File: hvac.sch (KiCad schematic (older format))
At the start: 35 parts, among them CN1 1X4-3.5MM, IC1 ATMEGA328P-A, J1 PROGRAMMING HEADER, J2 SERIAL PORT, J3 POWER_INPUT, J4 1X2-3.5MM, SW1 SPST, SW2 SPST, SW3 SPST, U1 MIC5225

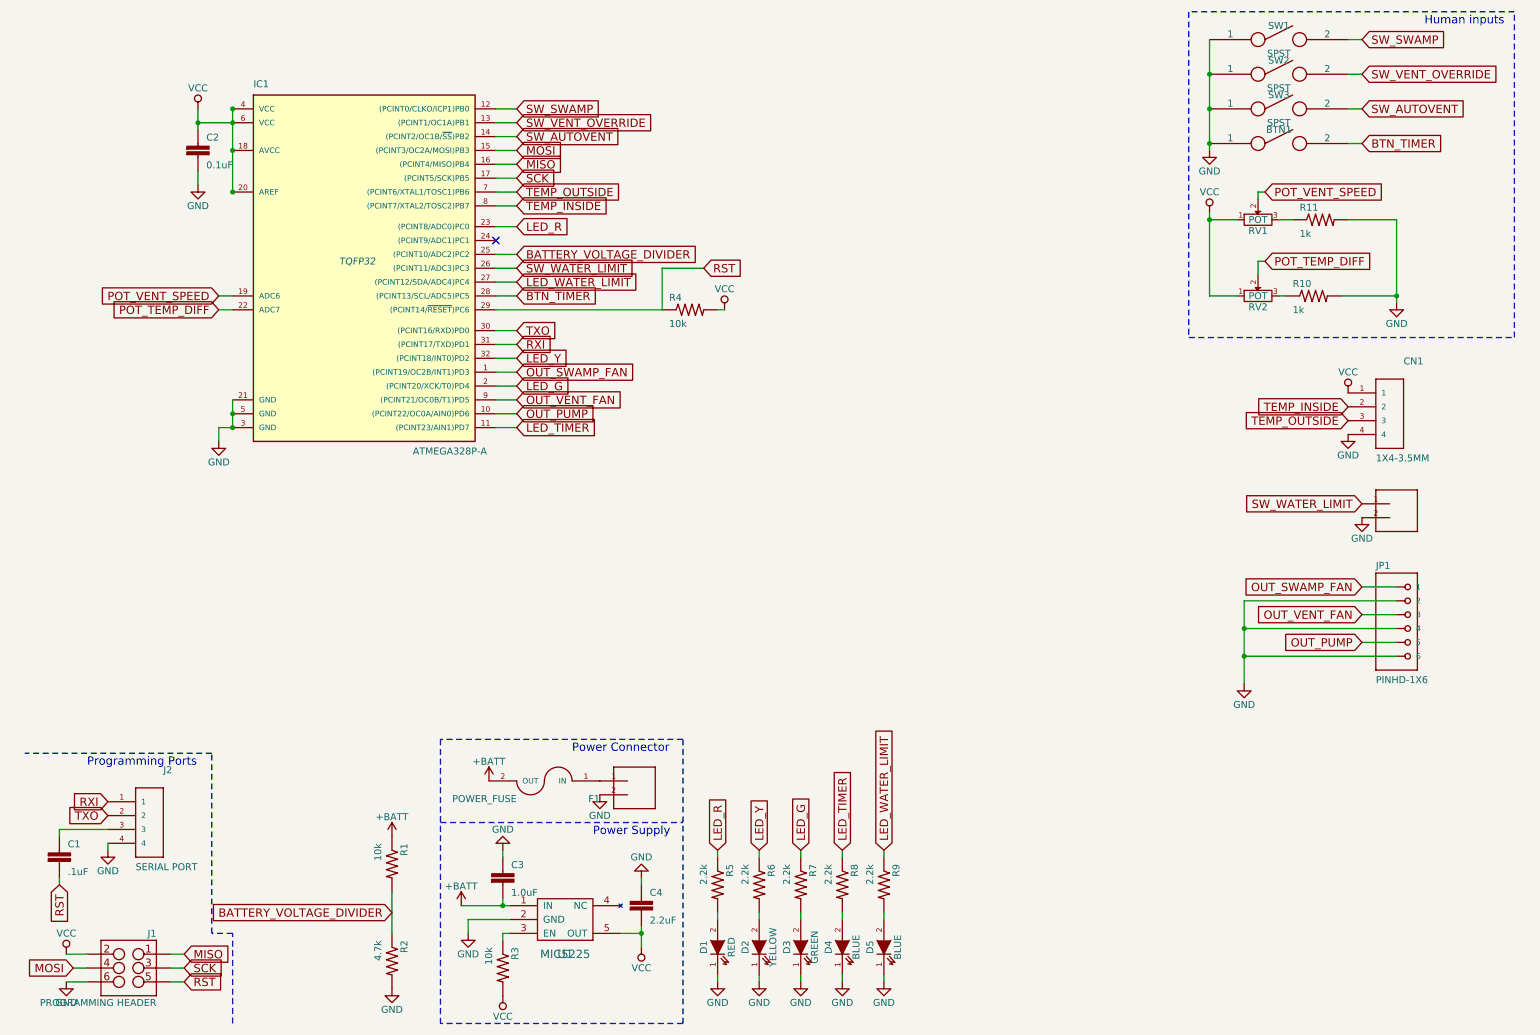
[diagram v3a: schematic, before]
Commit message: Add mosfets for driving fans and pump
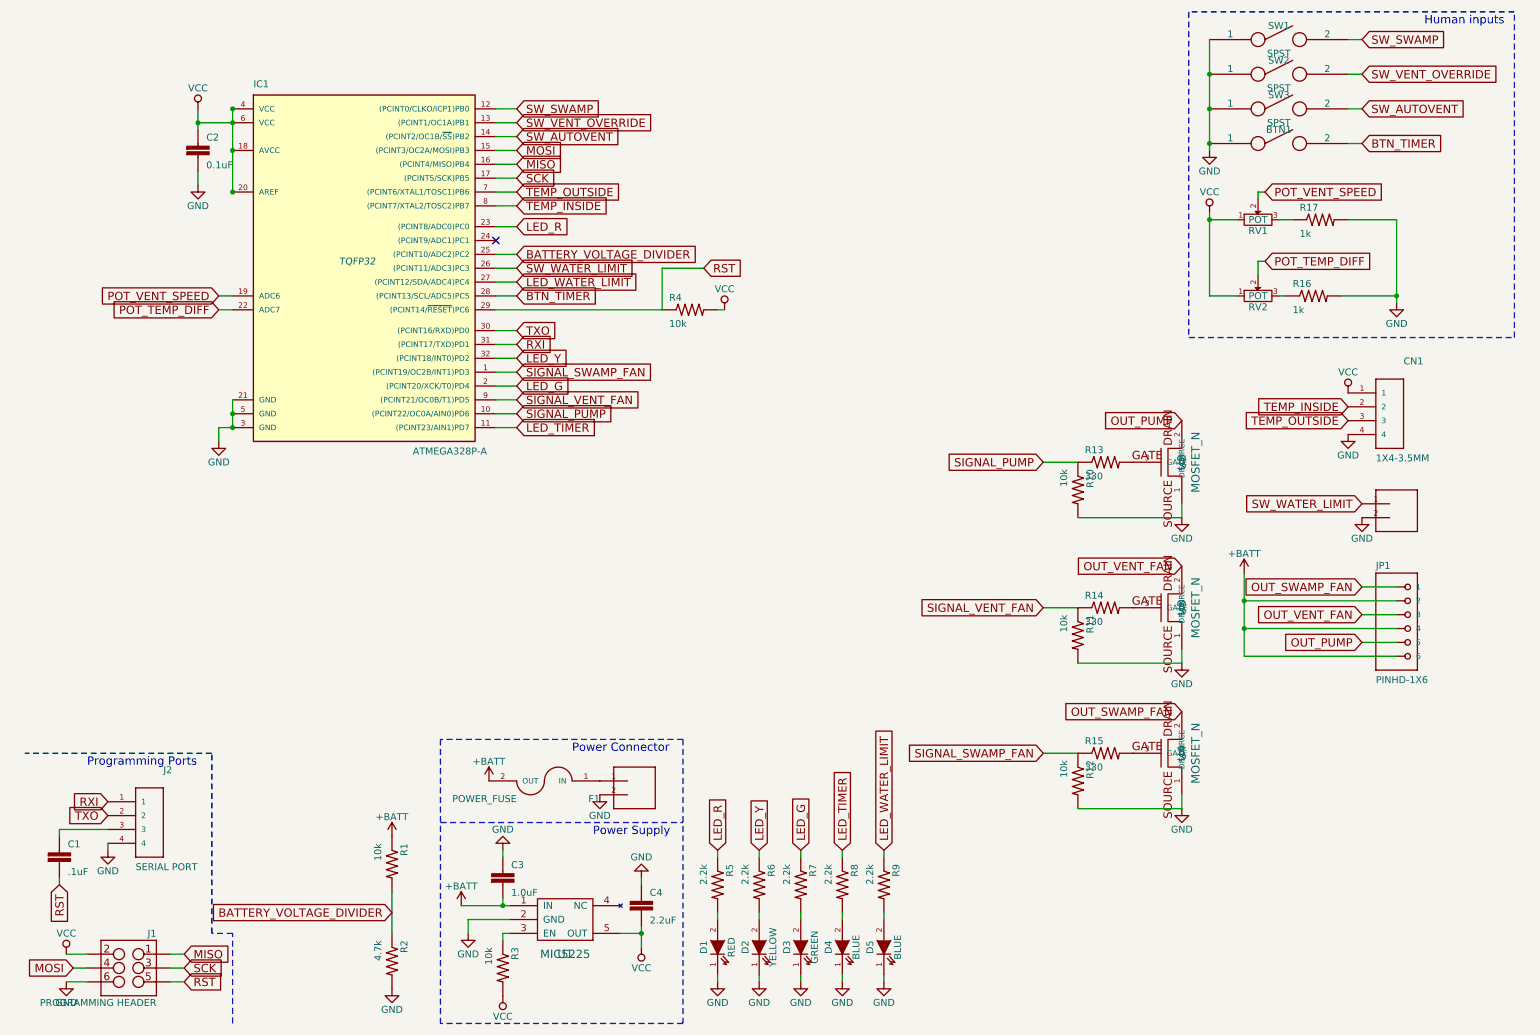
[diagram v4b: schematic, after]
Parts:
- added R10, R11, R12: 10k, 0402-RES, symbol RESISTOR0402
- added R13, R14, R15: 330, 0402-RES, symbol RESISTOR0402
- added U2, U3, U4: MOSFET_N, symbol MOSFET_N
- renumbered R10 to R16, R11 to R17
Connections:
- net +BATT: now also JP1.2, JP1.4, JP1.6
- net GND: now also R10.2, R11.2, R12.2, U2.1 (SOURCE), U3.1 (SOURCE), U4.1 (SOURCE); no longer JP1.2, JP1.4, JP1.6
- net OUT_PUMP: now also U2.2 (DRAIN); no longer IC1.10 ((PCINT22/OC0A/AIN0)PD6)
- net OUT_SWAMP_FAN: now also U4.2 (DRAIN); no longer IC1.1 ((PCINT19/OC2B/INT1)PD3)
- net OUT_VENT_FAN: now also U3.2 (DRAIN); no longer IC1.9 ((PCINT21/OC0B/T1)PD5)
- new net: R14.2, U3.3 (GATE)
- new net: R15.2, U4.3 (GATE)
- new net: R13.2, U2.3 (GATE)
- new net SIGNAL_PUMP: IC1.10 ((PCINT22/OC0A/AIN0)PD6), R10.1, R13.1
- new net SIGNAL_SWAMP_FAN: IC1.1 ((PCINT19/OC2B/INT1)PD3), R12.1, R15.1
- new net SIGNAL_VENT_FAN: IC1.9 ((PCINT21/OC0B/T1)PD5), R11.1, R14.1
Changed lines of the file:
@@
 	9350 1800 9400 1800
 $Comp
-L RESISTOR0402 R11
+L RESISTOR0402 R17
 U 1 1 590F04F0
 P 9800 2000
-F 0 "R11" H 9650 2059 50  0000 L BNN
+F 0 "R17" H 9650 2059 50  0000 L BNN
 F 1 "1k" H 9650 1870 50  0000 L BNN
 F 2 "0402-RES" H 9830 2150 20  0001 C CNN
@@
 	10350 2000 10000 2000
 $Comp
-L RESISTOR0402 R10
+L RESISTOR0402 R16
 U 1 1 590F06BC
 P 9750 2550
-F 0 "R10" H 9600 2609 50  0000 L BNN
+F 0 "R16" H 9600 2609 50  0000 L BNN
 F 1 "1k" H 9600 2420 50  0000 L BNN
 F 2 "0402-RES" H 9780 2700 20  0001 C CNN
@@
 	3850 3400 4000 3400
 Text GLabel 4000 3100 2    60   Input ~ 0
-OUT_SWAMP_FAN
+SIGNAL_SWAMP_FAN
 Text GLabel 4000 3300 2    60   Input ~ 0
-OUT_VENT_FAN
+SIGNAL_VENT_FAN
 Text GLabel 4000 3400 2    60   Input ~ 0
-OUT_PUMP
+SIGNAL_PUMP
 Text GLabel 4000 1200 2    60   Input ~ 0
 SW_SWAMP
@@
 Text GLabel 10100 4050 0    60   Input ~ 0
 SW_WATER_LIMIT
-Text GLabel 10100 4650 0    60   Input ~ 0
-OUT_SWAMP_FAN
+Text GLabel 7800 4800 0    60   Input ~ 0
+SIGNAL_VENT_FAN
 Text GLabel 10100 4850 0    60   Input ~ 0
 OUT_VENT_FAN
@@
 Wire Wire Line
 	10100 5050 10350 5050
-$Comp
-L GND #PWR029
-U 1 1 590FF3B2
-P 9250 5350
-F 0 "#PWR029" H 9250 5100 50  0001 C CNN
-F 1 "GND" H 9250 5200 50  0000 C CNN
-F 2 "" H 9250 5350 50  0000 C CNN
-F 3 "" H 9250 5350 50  0000 C CNN
-	1    9250 5350
-	1    0    0    -1
-$EndComp
-Wire Wire Line
-	9250 5350 9250 4750
-Wire Wire Line
-	9250 4750 10350 4750
-Wire Wire Line
-	10350 4950 9250 4950
-Connection ~ 9250 4950
-Wire Wire Line
-	10350 5150 9250 5150
-Connection ~ 9250 5150
 Connection ~ 9000 1450
 $Comp
@@
 	-1   0    0    1
 $EndComp
+$Comp
+L MOSFET_N U3
+U 1 1 59102281
+P 8900 4800
+F 0 "U3" H 8900 4900 60  0000 C CNN
+F 1 "MOSFET_N" H 8900 4800 60  0000 C CNN
+F 2 "" H 8900 4750 60  0000 C CNN
+F 3 "" H 8900 4750 60  0000 C CNN
+	1    8900 4800
+	0    -1   -1   0
+$EndComp
+$Comp
+L GND #PWR029
+U 1 1 59102A56
+P 8800 5200
+F 0 "#PWR029" H 8800 4950 50  0001 C CNN
+F 1 "GND" H 8800 5050 50  0000 C CNN
+F 2 "" H 8800 5200 50  0000 C CNN
+F 3 "" H 8800 5200 50  0000 C CNN
+	1    8800 5200
+	1    0    0    -1
+$EndComp
+$Comp
+L +BATT #PWR030
+U 1 1 59102C3A
+P 9250 4550
+F 0 "#PWR030" H 9250 4400 50  0001 C CNN
+F 1 "+BATT" H 9250 4690 50  0000 C CNN
+F 2 "" H 9250 4550 50  0000 C CNN
+F 3 "" H 9250 4550 50  0000 C CNN
+	1    9250 4550
+	1    0    0    -1
+$EndComp
+$Comp
+L RESISTOR0402 R14
+U 1 1 59102F73
+P 8250 4800
+F 0 "R14" H 8100 4859 50  0000 L BNN
+F 1 "330" H 8100 4670 50  0000 L BNN
+F 2 "0402-RES" H 8280 4950 20  0001 C CNN
+F 3 "" H 8250 4800 60  0000 C CNN
+	1    8250 4800
+	1    0    0    -1
+$EndComp
+$Comp
+L RESISTOR0402 R11
+U 1 1 591032B1
+P 8050 5000
+F 0 "R11" H 7900 5059 50  0000 L BNN
+F 1 "10k" H 7900 4870 50  0000 L BNN
+F 2 "0402-RES" H 8080 5150 20  0001 C CNN
+F 3 "" H 8050 5000 60  0000 C CNN
+	1    8050 5000
+	0    1    1    0
+$EndComp
+Wire Wire Line
+	7800 4800 8050 4800
+Text GLabel 8800 4500 0    60   Input ~ 0
+OUT_VENT_FAN
+Text GLabel 10100 4650 0    60   Input ~ 0
+OUT_SWAMP_FAN
+Wire Wire Line
+	9250 4550 9250 5150
+Wire Wire Line
+	9250 5150 10350 5150
+Wire Wire Line
+	10350 4950 9250 4950
+Connection ~ 9250 4950
+Wire Wire Line
+	9250 4750 10350 4750
+Connection ~ 9250 4750
+Wire Wire Line
+	8800 5100 8800 5200
+Text GLabel 7800 5850 0    60   Input ~ 0
+SIGNAL_SWAMP_FAN
+$Comp
+L MOSFET_N U4
+U 1 1 591065E0
+P 8900 5850
+F 0 "U4" H 8900 5950 60  0000 C CNN
+F 1 "MOSFET_N" H 8900 5850 60  0000 C CNN
+F 2 "" H 8900 5800 60  0000 C CNN
+F 3 "" H 8900 5800 60  0000 C CNN
+	1    8900 5850
+	0    -1   -1   0
+$EndComp
+$Comp
+L GND #PWR031
+U 1 1 591065E6
+P 8800 6250
+F 0 "#PWR031" H 8800 6000 50  0001 C CNN
+F 1 "GND" H 8800 6100 50  0000 C CNN
+F 2 "" H 8800 6250 50  0000 C CNN
+F 3 "" H 8800 6250 50  0000 C CNN
+	1    8800 6250
+	1    0    0    -1
+$EndComp
+$Comp
+L RESISTOR0402 R15
+U 1 1 591065EC
+P 8250 5850
+F 0 "R15" H 8100 5909 50  0000 L BNN
+F 1 "330" H 8100 5720 50  0000 L BNN
+F 2 "0402-RES" H 8280 6000 20  0001 C CNN
+F 3 "" H 8250 5850 60  0000 C CNN
+	1    8250 5850
+	1    0    0    -1
+$EndComp
+$Comp
+L RESISTOR0402 R12
+U 1 1 591065F2
+P 8050 6050
+F 0 "R12" H 7900 6109 50  0000 L BNN
+F 1 "10k" H 7900 5920 50  0000 L BNN
+F 2 "0402-RES" H 8080 6200 20  0001 C CNN
+F 3 "" H 8050 6050 60  0000 C CNN
+	1    8050 6050
+	0    1    1    0
+$EndComp
+Wire Wire Line
+	7800 5850 8050 5850
+Text GLabel 8800 5550 0    60   Input ~ 0
+OUT_SWAMP_FAN
+Wire Wire Line
+	8800 6250 8050 6250
+Wire Wire Line
+	8800 6150 8800 6250
+Text GLabel 7800 3750 0    60   Input ~ 0
+SIGNAL_PUMP
+$Comp
+L MOSFET_N U2
+U 1 1 591067AD
+P 8900 3750
+F 0 "U2" H 8900 3850 60  0000 C CNN
+F 1 "MOSFET_N" H 8900 3750 60  0000 C CNN
+F 2 "" H 8900 3700 60  0000 C CNN
+F 3 "" H 8900 3700 60  0000 C CNN
+	1    8900 3750
+	0    -1   -1   0
+$EndComp
+$Comp
+L GND #PWR032
+U 1 1 591067B3
+P 8800 4150
+F 0 "#PWR032" H 8800 3900 50  0001 C CNN
+F 1 "GND" H 8800 4000 50  0000 C CNN
+F 2 "" H 8800 4150 50  0000 C CNN
+F 3 "" H 8800 4150 50  0000 C CNN
+	1    8800 4150
+	1    0    0    -1
+$EndComp
+$Comp
+L RESISTOR0402 R13
+U 1 1 591067B9
+P 8250 3750
+F 0 "R13" H 8100 3809 50  0000 L BNN
+F 1 "330" H 8100 3620 50  0000 L BNN
+F 2 "0402-RES" H 8280 3900 20  0001 C CNN
+F 3 "" H 8250 3750 60  0000 C CNN
+	1    8250 3750
+	1    0    0    -1
+$EndComp
+$Comp
+L RESISTOR0402 R10
+U 1 1 591067BF
+P 8050 3950
+F 0 "R10" H 7900 4009 50  0000 L BNN
+F 1 "10k" H 7900 3820 50  0000 L BNN
+F 2 "0402-RES" H 8080 4100 20  0001 C CNN
+F 3 "" H 8050 3950 60  0000 C CNN
+	1    8050 3950
+	0    1    1    0
+$EndComp
+Wire Wire Line
+	7800 3750 8050 3750
+Text GLabel 8800 3450 0    60   Input ~ 0
+OUT_PUMP
+Wire Wire Line
+	8800 4150 8050 4150
+Wire Wire Line
+	8800 4050 8800 4150
+Wire Wire Line
+	8800 5200 8050 5200
 $EndSCHEMATC

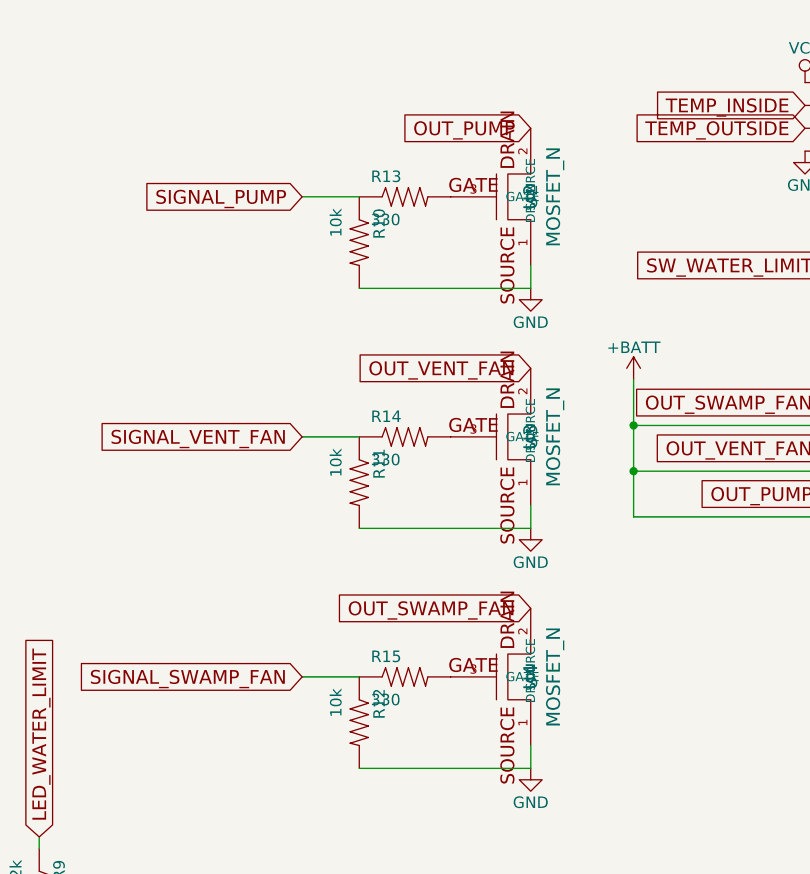
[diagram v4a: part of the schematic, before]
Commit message: Switch to 220ohm resistors
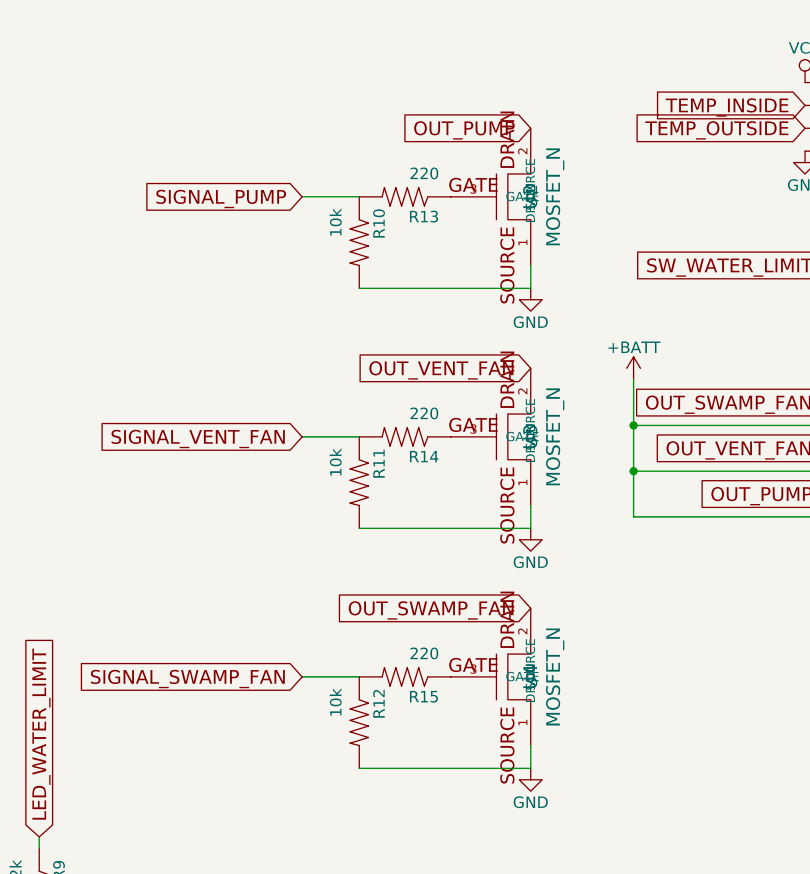
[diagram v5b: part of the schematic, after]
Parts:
- R13, R14, R15: value 330 -> 220
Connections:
- net SIGNAL_PUMP: now also R13.2; no longer R13.1
- net SIGNAL_SWAMP_FAN: now also R15.2; no longer R15.1
- net SIGNAL_VENT_FAN: now also R14.2; no longer R14.1
- net at U3.3 (GATE): now also R14.1; no longer R14.2
- net at U4.3 (GATE): now also R15.1; no longer R15.2
- net at U2.3 (GATE): now also R13.1; no longer R13.2
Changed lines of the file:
@@
 P 8250 4800
 F 0 "R14" H 8100 4859 50  0000 L BNN
-F 1 "330" H 8100 4670 50  0000 L BNN
+F 1 "220" H 8100 4670 50  0000 L BNN
 F 2 "0402-RES" H 8280 4950 20  0001 C CNN
 F 3 "" H 8250 4800 60  0000 C CNN
 	1    8250 4800
-	1    0    0    -1
+	-1   0    0    1
 $EndComp
 $Comp
@@
 P 8250 5850
 F 0 "R15" H 8100 5909 50  0000 L BNN
-F 1 "330" H 8100 5720 50  0000 L BNN
+F 1 "220" H 8100 5720 50  0000 L BNN
 F 2 "0402-RES" H 8280 6000 20  0001 C CNN
 F 3 "" H 8250 5850 60  0000 C CNN
 	1    8250 5850
-	1    0    0    -1
+	-1   0    0    1
 $EndComp
 $Comp
@@
 P 8250 3750
 F 0 "R13" H 8100 3809 50  0000 L BNN
-F 1 "330" H 8100 3620 50  0000 L BNN
+F 1 "220" H 8100 3620 50  0000 L BNN
 F 2 "0402-RES" H 8280 3900 20  0001 C CNN
 F 3 "" H 8250 3750 60  0000 C CNN
 	1    8250 3750
-	1    0    0    -1
+	-1   0    0    1
 $EndComp
 $Comp
